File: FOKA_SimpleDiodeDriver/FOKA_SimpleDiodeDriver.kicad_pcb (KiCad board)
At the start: 2 copper layers, 30 x 30 mm, 25 parts, among them J1 IN, J2 Conn_01x02, Q2 BJT, U2 ADA4891-1

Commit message: v0.9
awaiting pre-production review
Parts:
- J2: footprint Connector_Phoenix_MC_HighVoltage:PhoenixContact_MC_1,5_2-G-5.08_1x02_P5.08mm_Horizontal -> Power_Connectors:691313510002
- REF**: moved to F.Cu
- moved REF** 10.8 mm to (119.5, 59.5), turned to 0 degrees
- moved J2 0.50 mm to (107.5, 52.0)
- moved REF** 0.28 mm to (109.7, 66.7)
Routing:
- net Net-(J1-In): track 4.81 -> 3.92 mm

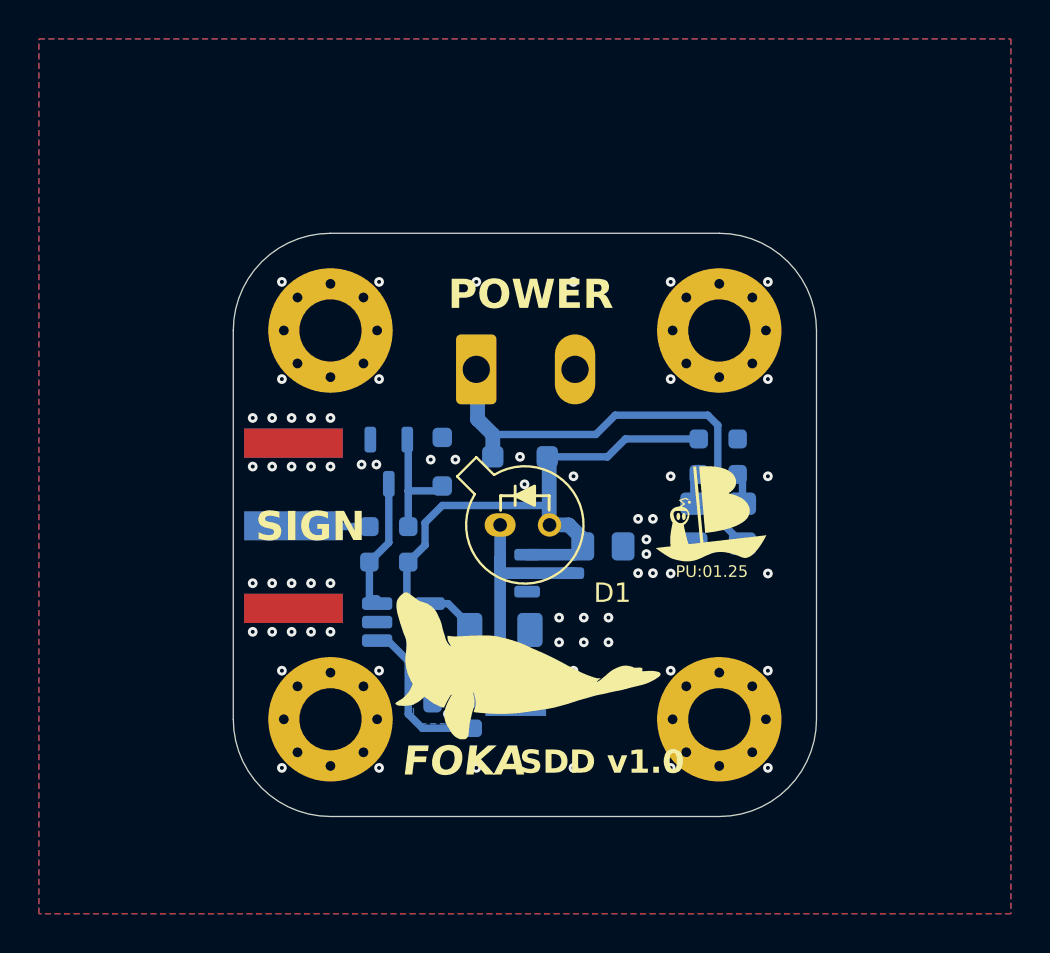
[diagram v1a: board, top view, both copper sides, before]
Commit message: recommended changes
voltage reference as OC prot.
layout changes
made vias bigger
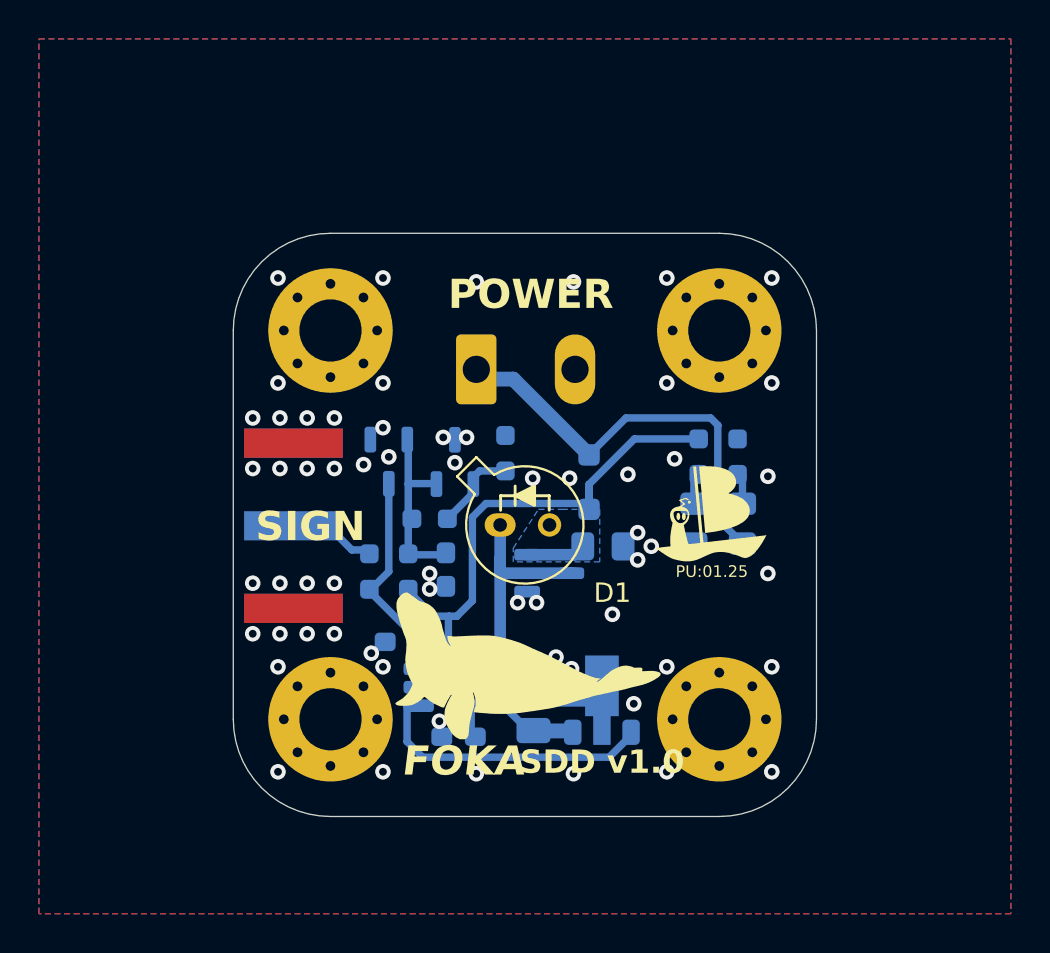
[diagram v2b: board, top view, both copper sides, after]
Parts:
- removed D4: 2V5, Diode_SMD:D_SOD-323_HandSoldering
- added C3: 1u, Capacitor_SMD:C_0603_1608Metric_Pad1.08x0.95mm_HandSolder, B.Cu at (105.9, 62.3)
- added C4: 10p, Capacitor_SMD:C_0603_1608Metric_Pad1.08x0.95mm_HandSolder, B.Cu at (103.7, 66.0)
- added R6: 10k, Resistor_SMD:R_0603_1608Metric_Pad0.98x0.95mm_HandSolder, B.Cu at (105.1, 59.7)
- added R7: 15k, Resistor_SMD:R_0603_1608Metric_Pad0.98x0.95mm_HandSolder, B.Cu at (109.0, 56.3)
- added U1: AZ431L, Package_TO_SOT_SMD:SOT-23-3, B.Cu at (106.4, 56.8)
- C1: value 1u -> 10u
- C2: value 100n -> 1u
- D1: value LED -> IR LED
- R2: value R -> 3k
- R3, R4, R5: value R -> 1k5
- moved Q2 4.88 mm to (114.0, 68.7), turned to 90 degrees
- moved R1 4.02 mm to (110.4, 69.0), turned to 90 degrees
- moved U2 3.97 mm to (105.9, 68.3)
- moved D6 3.78 mm to (113.3, 57.8), turned to 90 degrees
- moved C2 2.97 mm to (106.6, 70.9), turned to 180 degrees
- moved R2 1.40 mm to (104.0, 62.4)
- moved R3 1.40 mm to (102.0, 62.4)
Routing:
- net Net-(Q2-B): track 8.21 -> 15.0 mm
- net Net-(D1-K): track 17.9 -> 24.0 mm
- net Net-(U1-REF): track 0.00 -> 4.80 mm
- net Net-(D3A-K): track 6.73 -> 11.0 mm
- net Net-(U1-K): track 6.75 -> 9.41 mm
- net Net-(Q2-E): track 4.83 -> 7.08 mm
- net Net-(D6-A): track 23.2 -> 21.6 mm
- net VCC: track 32.8 -> 33.9 mm
- net GND: vias 67 -> 63
- added copper zone on B.Cu, net VCC

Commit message: BJT -> NMOS
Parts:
- Q2: value BJT -> NMOS
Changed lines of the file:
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@@
 			)
 		)
-		(property "Value" "BJT"
+		(property "Value" "NMOS"
 			(at 0 -3.5 90)
 			(layer "B.Fab")
@@
 			)
 		)
-		(property "Description" "NPN transistor, base/collector/emitter"
+		(property "Description" "N-MOSFET transistor, gate/drain/source"
 			(at 0 0 270)
 			(unlocked yes)
@@
 			(roundrect_rratio 0.25)
 			(net 4 "Net-(Q2-B)")
-			(pinfunction "B")
+			(pinfunction "G")
 			(pintype "input")
 		)
@@
 			(layers "B.Cu" "B.Mask" "B.Paste")
 			(net 3 "Net-(D1-K)")
-			(pinfunction "C")
+			(pinfunction "D")
 			(pintype "passive")
 			(zone_connect 2)
@@
 			(roundrect_rratio 0.25)
 			(net 6 "Net-(Q2-E)")
-			(pinfunction "E")
+			(pinfunction "S")
 			(pintype "passive")
 		)

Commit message: Humpback update drop
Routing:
- net Net-(D1-K): vias 0 -> 7
- added copper zone on B.Cu, net Net-(D1-K)
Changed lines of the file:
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@@
 	)
 	(via
-		(at 114.5 64.6)
+		(at 113.3 64.9)
 		(size 0.8)
 		(drill 0.4)
@@
 	)
 	(via
-		(at 115.6 69.2)
+		(at 115.9 69.2)
 		(size 0.8)
 		(drill 0.4)
@@
 		(layer "B.Cu")
 		(net 2)
+	)
+	(via
+		(at 119 63.5)
+		(size 0.6)
+		(drill 0.3)
+		(layers "F.Cu" "B.Cu")
+		(free yes)
+		(net 3)
+	)
+	(via
+		(at 121 65.5)
+		(size 0.6)
+		(drill 0.3)
+		(layers "F.Cu" "B.Cu")
+		(free yes)
+		(net 3)
+	)
+	(via
+		(at 117 63.5)
+		(size 0.6)
+		(drill 0.3)
+		(layers "F.Cu" "B.Cu")
+		(free yes)
+		(net 3)
+	)
+	(via
+		(at 119 65.5)
+		(size 0.6)
+		(drill 0.3)
+		(layers "F.Cu" "B.Cu")
+		(free yes)
+		(net 3)
+	)
+	(via
+		(at 115 65.5)
+		(size 0.6)
+		(drill 0.3)
+		(layers "F.Cu" "B.Cu")
+		(free yes)
+		(net 3)
+	)
+	(via
+		(at 117 65.5)
+		(size 0.6)
+		(drill 0.3)
+		(layers "F.Cu" "B.Cu")
+		(free yes)
+		(net 3)
+	)
+	(via
+		(at 121 63.5)
+		(size 0.6)
+		(drill 0.3)
+		(layers "F.Cu" "B.Cu")
+		(free yes)
+		(net 3)
 	)
 	(segment
@@
 			)
 		)
+	)
+	(zone
+		(net 3)
+		(net_name "Net-(D1-K)")
+		(layer "B.Cu")
+		(hatch edge 0.5)
+		(priority 2)
+		(connect_pads yes
+			(clearance 0)
+		)
+		(min_thickness 0.25)
+		(filled_areas_thickness no)
+		(fill yes
+			(thermal_gap 0.5)
+			(thermal_bridge_width 0.5)
+		)
+		(polygon
+			(pts
+				(xy 113 69.8) (xy 113 66.6) (xy 115.769231 62.6) (xy 122 62.6) (xy 122.7 63.3) (xy 122.7 65.5) (xy 121.9 66.3)
+				(xy 116.881081 66.3) (xy 114.8 69.8)
+			)
+		)

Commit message: Final?
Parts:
- added C5: optional, Capacitor_SMD:C_0402_1005Metric, B.Cu at (107.8, 65.7)
- added R8: 1M, Resistor_SMD:R_0603_1608Metric_Pad0.98x0.95mm_HandSolder, F.Cu at (102.4, 59.5)
- added R9: optional, Capacitor_SMD:C_0402_1005Metric, B.Cu at (108.8, 69.8)
- R1: value 10R -> 1R
- R3: value 1k5 -> 100
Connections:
- Q2 pad 3: Net-(Q2-E) -> Net-(Q2-S)
- R1 pad 1: Net-(Q2-E) -> Net-(Q2-S)
- U2 pad 4: Net-(Q2-E) -> Net-(U2--)
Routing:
- net Net-(Q2-E): track 7.08 -> 0.00 mm
- net Net-(U2--): track 0.00 -> 4.66 mm
- net Net-(Q2-S): track 0.00 -> 4.13 mm
- net Net-(D3A-K): track 11.0 -> 12.6 mm, vias 0 -> 1
- net GND: vias 63 -> 64
- added copper zone on F.Cu, net Net-(D1-K)

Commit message: RezystorDoBramki
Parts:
- added R10: optional, Capacitor_SMD:C_0402_1005Metric, B.Cu at (115.0, 72.0)
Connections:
- U2 pad 1: Net-(Q2-G) -> Net-(R10-Pad1)
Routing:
- net Net-(Q2-G): track 15.0 -> 1.53 mm
- net Net-(R10-Pad1): track 0.00 -> 13.4 mm
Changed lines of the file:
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@@
 	(net 12 "Net-(U1-REF)")
 	(net 13 "Net-(Q2-S)")
+	(net 14 "Net-(R10-Pad1)")
 	(footprint "Package_TO_SOT_THT:TO-18-2_Window"
 		(layer "F.Cu")
@@
 			(layers "B.Cu" "B.Mask" "B.Paste")
 			(roundrect_rratio 0.25)
-			(net 6 "Net-(Q2-G)")
+			(net 14 "Net-(R10-Pad1)")
 			(pintype "output")
 		)
@@
 		)
 	)
+	(footprint "Capacitor_SMD:C_0402_1005Metric"
+		(layer "B.Cu")
+		(at 115.035 71.985)
+		(descr "Capacitor SMD 0402 (1005 Metric), square (rectangular) end terminal, IPC-7351 nominal, (Body size source: IPC-SM-782 page 76, https://www.pcb-3d.com/wordpress/wp-content/uploads/ipc-sm-782a_amendment_1_and_2.pdf), generated with kicad-footprint-generator")
+		(tags "capacitor")
+		(property "Reference" "R10"
+			(at -2.335 0.015 0)
+			(layer "B.SilkS")
+			(effects
+				(font
+					(size 1 1)
+					(thickness 0.15)
+				)
+				(justify mirror)
+			)
+		)
+		(property "Value" "optional"
+			(at 0 -1.16 0)
+			(layer "B.Fab")
+			(effects
+				(font
+					(size 1 1)
+					(thickness 0.15)
+				)
+				(justify mirror)
+			)
+		)
+		(property "Datasheet" ""
+			(at 0 0 0)
+			(layer "B.Fab")
+			(hide yes)
+			(effects
+				(font
+					(size 1.27 1.27)
+					(thickness 0.15)
+				)
+				(justify mirror)
+			)
+		)
+		(property "Description" "Resistor"
+			(at 0 0 0)
+			(layer "B.Fab")
+			(hide yes)
+			(effects
+				(font
+					(size 1.27 1.27)
+					(thickness 0.15)
+				)
+				(justify mirror)
+			)
+		)
+		(property ki_fp_filters "R_*")
+		(sheetname "/")
+		(sheetfile "FOKA_SimpleDiodeDriver.kicad_sch")
+		(attr smd)
+		(fp_line
+			(start -0.107836 -0.36)
+			(end 0.107836 -0.36)
+			(stroke
+				(width 0.12)
+				(type solid)
+			)
+			(layer "B.SilkS")
+		)
+		(fp_line
+			(start -0.107836 0.36)
+			(end 0.107836 0.36)
+			(stroke
+				(width 0.12)
+				(type solid)
+			)
+			(layer "B.SilkS")
+		)
+		(fp_line
+			(start -0.91 -0.46)
+			(end -0.91 0.46)
+			(stroke
+				(width 0.05)
+				(type solid)
+			)
+			(layer "B.CrtYd")
+		)
+		(fp_line
+			(start -0.91 0.46)
+			(end 0.91 0.46)
+			(stroke
+				(width 0.05)
+				(type solid)
+			)
+			(layer "B.CrtYd")
+		)
+		(fp_line
+			(start 0.91 -0.46)
+			(end -0.91 -0.46)
+			(stroke
+				(width 0.05)
+				(type solid)
+			)
+			(layer "B.CrtYd")
+		)
+		(fp_line
+			(start 0.91 0.46)
+			(end 0.91 -0.46)
+			(stroke
+				(width 0.05)
+				(type solid)
+			)
+			(layer "B.CrtYd")
+		)
+		(fp_line
+			(start -0.5 -0.25)
+			(end -0.5 0.25)
+			(stroke
+				(width 0.1)
+				(type solid)
+			)
+			(layer "B.Fab")
+		)
+		(fp_line
+			(start -0.5 0.25)
+			(end 0.5 0.25)
+			(stroke
+				(width 0.1)
+				(type solid)
+			)
+			(layer "B.Fab")
+		)
+		(fp_line
+			(start 0.5 -0.25)
+			(end -0.5 -0.25)
+			(stroke
+				(width 0.1)
+				(type solid)
+			)
+			(layer "B.Fab")
+		)
+		(fp_line
+			(start 0.5 0.25)
+			(end 0.5 -0.25)
+			(stroke
+				(width 0.1)
+				(type solid)
+			)
+			(layer "B.Fab")
+		)
+		(fp_text user "${REFERENCE}"
+			(at 0 0 0)
+			(layer "B.Fab")
+			(effects
+				(font
+					(size 0.25 0.25)
+					(thickness 0.04)
+				)
+				(justify mirror)
+			)
+		)
+		(pad "1" smd roundrect
+			(at -0.48 0)
+			(size 0.56 0.62)
+			(layers "B.Cu" "B.Mask" "B.Paste")
+			(roundrect_rratio 0.25)
+			(net 14 "Net-(R10-Pad1)")
+			(pintype "passive")
+		)
+		(pad "2" smd roundrect
+			(at 0.48 0)
+			(size 0.56 0.62)
+			(layers "B.Cu" "B.Mask" "B.Paste")
+			(roundrect_rratio 0.25)
+			(net 6 "Net-(Q2-G)")
+			(pintype "passive")
+		)
+		(embedded_fonts no)
+		(model "${KICAD9_3DMODEL_DIR}/Capacitor_SMD.3dshapes/C_0402_1005Metric.step"
+			(offset
+				(xyz 0 0 0)
+			)
+			(scale
+				(xyz 1 1 1)
+			)
+			(rotate
+				(xyz 0 0 0)
+			)
+		)
+	)
 	(footprint "Resistor_SMD:R_0603_1608Metric_Pad0.98x0.95mm_HandSolder"
 		(layer "B.Cu")
@@
 	)
 	(segment
-		(start 103.9375 71.15)
-		(end 104.7375 71.95)
-		(width 0.381)
-		(layer "B.Cu")
-		(net 6)
-	)
-	(segment
-		(start 103.9375 69.3)
-		(end 103.9375 71.15)
-		(width 0.381)
-		(layer "B.Cu")
-		(net 6)
-	)
-	(segment
-		(start 104.7375 71.95)
-		(end 114.3375 71.95)
+		(start 115.515 70.718843)
+		(end 115.4625 70.666343)
 		(width 0.381)
 		(layer "B.Cu")
@@
 	)
 	(segment
-		(start 115.5 70.7875)
-		(end 115.5 70.6)
-		(width 0.381)
-		(layer "B.Cu")
-		(net 6)
-	)
-	(segment
-		(start 104.5375 69.3)
-		(end 103.9375 69.3)
+		(start 115.5 70.6)
+		(end 115.5 70.7875)
 		(width 0.381)
 		(layer "B.Cu")
@@
 	)
 	(segment
-		(start 114.3375 71.95)
-		(end 115.5 70.7875)
+		(start 115.515 71.985)
+		(end 115.515 70.718843)
 		(width 0.381)
 		(layer "B.Cu")
@@
 		(net 13)
 	)
+	(segment
+		(start 103.9375 71.15)
+		(end 104.7725 71.985)
+		(width 0.381)
+		(layer "B.Cu")
+		(net 14)
+	)
+	(segment
+		(start 104.5375 69.3)
+		(end 103.9375 69.3)
+		(width 0.381)
+		(layer "B.Cu")
+		(net 14)
+	)
+	(segment
+		(start 104.7725 71.985)
+		(end 114.555 71.985)
+		(width 0.381)
+		(layer "B.Cu")
+		(net 14)
+	)
+	(segment
+		(start 103.9375 69.3)
+		(end 103.9375 71.15)
+		(width 0.381)
+		(layer "B.Cu")
+		(net 14)
+	)
 	(zone
